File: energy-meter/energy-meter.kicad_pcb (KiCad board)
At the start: 2 copper layers, 82 x 62.5 mm, 74 parts, among them J1 Screw_Terminal_01x04, J2 Conn_01x03, J3 I2C OLED Display, etc., K1 G5RL-U1A-E, K2 DNP / HF3FF/005-1HST, P1 PineNut, Q1 AP3400, T1 AP-2500, T2 BV 202 0154, T3 DNP / AP-2500, U1 L9110S, U11 SLG47004, U2 MCP6V96T-E/OT, U9 GD32VF103

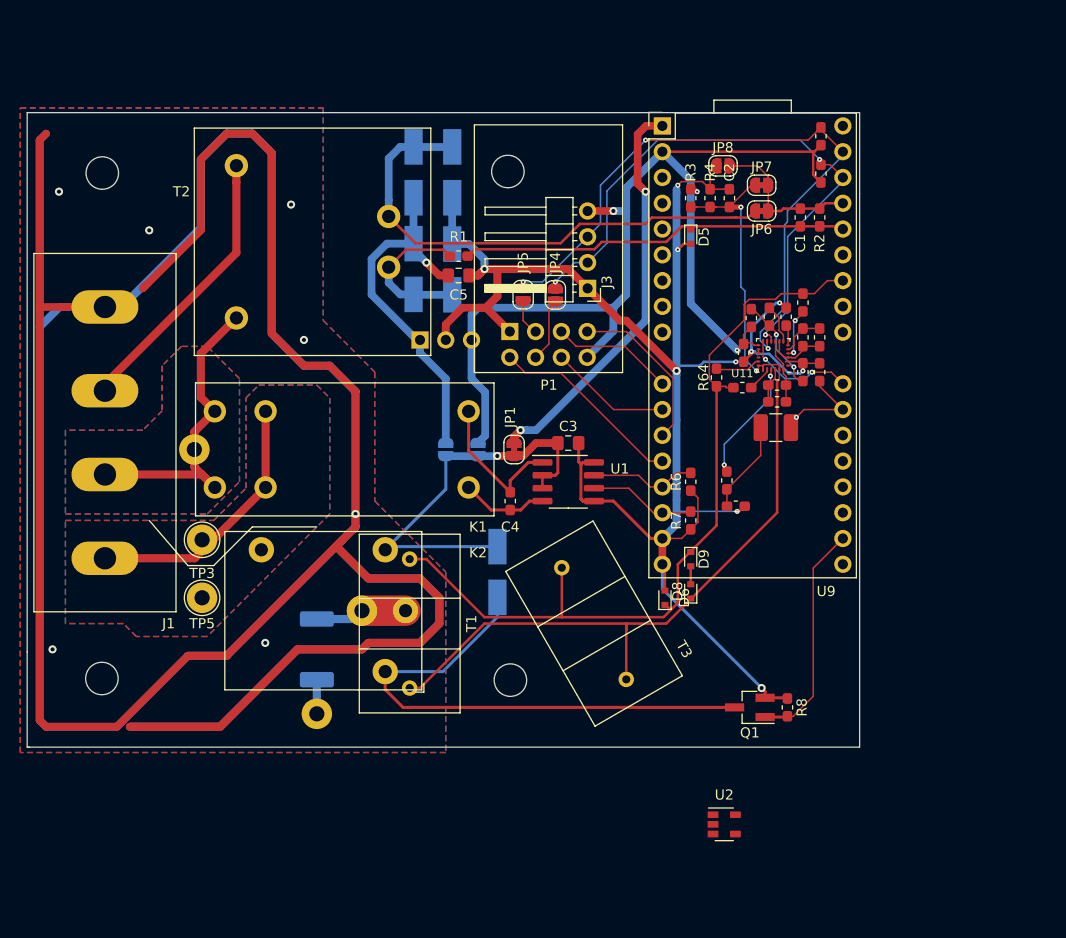
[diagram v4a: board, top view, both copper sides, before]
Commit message: use solid state relays for calibration
That way, we have enough space for two of them. The alternative relay
shares space with the other relay because only one of them will be used.
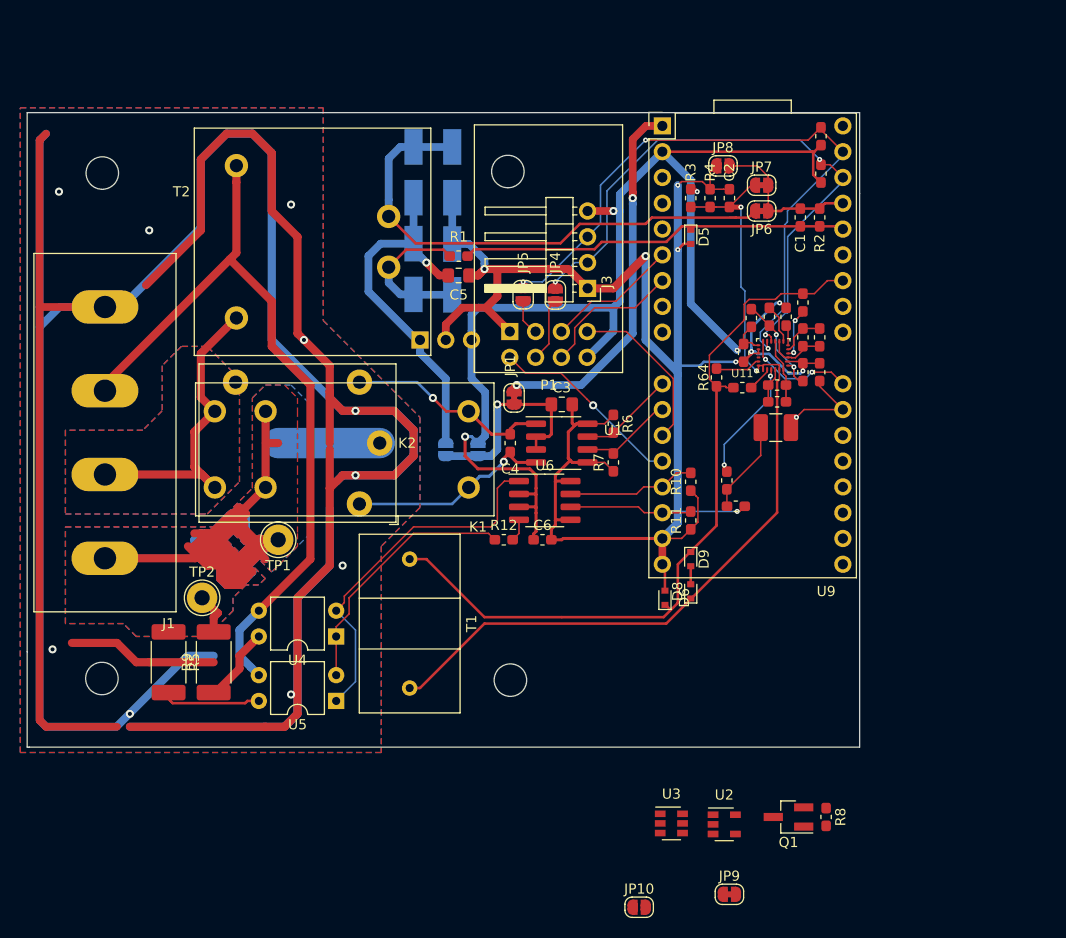
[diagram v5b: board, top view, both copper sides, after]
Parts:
- removed D7: D_Schottky, Diode_SMD:D_SMA_Handsoldering
- removed T3: DNP / AP-2500, energy-meter:AP-2500
- removed the TP2 at (119.5, 126.5)
- removed TP3, TP4: TestPoint, TestPoint:TestPoint_THTPad_D3.0mm_Drill1.5mm
- added C6: 100n, Capacitor_SMD:C_0603_1608Metric_Pad1.05x0.95mm_HandSolder, F.Cu at (153.8, 135.4)
- added JP10: SolderJumper_2_Open, Jumper:SolderJumper-2_P1.3mm_Open_RoundedPad1.0x1.5mm, F.Cu at (163.3, 171.6)
- added JP9: SolderJumper_2_Bridged, Jumper:SolderJumper-2_P1.3mm_Bridged_RoundedPad1.0x1.5mm, F.Cu at (172.2, 170.3)
- added NT2: Net-Tie_2, NetTie:NetTie-2_SMD_Pad2.0mm, F.Cu at (122.1, 134.8)
- added NT3: Net-Tie_2, NetTie:NetTie-2_SMD_Pad2.0mm, F.Cu at (124.6, 137.3)
- added NT4: Net-Tie_2, NetTie:NetTie-2_SMD_Pad2.0mm, B.Cu at (122.1, 134.8)
- added NT5: Net-Tie_2, NetTie:NetTie-2_SMD_Pad2.0mm, B.Cu at (124.6, 137.3)
- added R10: 10k, Resistor_SMD:R_0603_1608Metric_Pad1.05x0.95mm_HandSolder, F.Cu at (168.4, 129.7)
- added R11: 10k, Resistor_SMD:R_0603_1608Metric_Pad1.05x0.95mm_HandSolder, F.Cu at (168.4, 133.5)
- added R12: 120R, Resistor_SMD:R_0603_1608Metric_Pad1.05x0.95mm_HandSolder, F.Cu at (150.0, 135.4)
- added R9: 470kOhm, 0.1W, 1%, Resistor_SMD:R_2512_6332Metric_Pad1.52x3.35mm_HandSolder, F.Cu at (121.4, 147.5)
- added U3: TS5A3159ADBVR, Package_TO_SOT_SMD:SOT-23-6, F.Cu at (166.5, 163.3)
- added U4: EPR211A354001EZ, Package_DIP:DIP-4_W7.62mm, F.Cu at (133.5, 144.9)
- added U5: EPR211A354001EZ, Package_DIP:DIP-4_W7.62mm, F.Cu at (133.5, 151.3)
- added U6: L9110S, Package_SO:SOP-8_3.76x4.96mm_P1.27mm, F.Cu at (154.1, 131.5)
- R5: value 39kOhm, 2W, 1% -> 27kOhm, 2W, 1%; moved to F.Cu
- TP1: moved to F.Cu
- moved K2 16.7 mm to (129.7, 125.9)
- moved R5 14.7 mm to (117.0, 147.5)
- moved Q1 11.4 mm to (178.1, 162.7)
- moved R8 11.4 mm to (181.8, 162.7)
- moved TP1 10.8 mm to (127.8, 135.4)
- moved R6 9.52 mm to (160.8, 124.0), turned to 270 degrees
- moved R7 9.52 mm to (160.8, 127.8)
- moved C4 5.71 mm to (150.7, 125.9)
- moved JP1 5.08 mm to (151.0, 121.4)
- moved C3 3.86 mm to (155.7, 122.1)
- moved U1 3.86 mm to (155.7, 125.9)
- renumbered NT2 to NT1, TP5 to TP2
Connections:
- J1 pad 4: L_OUT -> L_OUT2
- K2 pad 1: Net-(K2-Pad1) -> L_OUT
- K2 pad 14: Net-(K2-Pad1) -> L_OUT
- K2 pad 2: /VCC_COIL -> /coil+
- K2 pad 6: Net-(D7-Pad2) -> /coil-
- K2 pad 7: L_OUT -> L_IN
- K2 pad 8: L_OUT -> L_IN
- Q1 pad 1: /RELAY2 -> /Calibration circuits for 230V/RELAY2
- Q1 pad 3: Net-(D7-Pad2) -> Net-(Q1-Pad3)
- R5 pad 2: Net-(K2-Pad1) -> L_OUT2
- R8 pad 2: /RELAY2 -> /Calibration circuits for 230V/RELAY2
- TP1 pad 1: Net-(K2-Pad1) -> L_OUT
- TP2 pad 1: L_OUT -> L_OUT2
- U9 pad 11: /PINENUT_IO8_BOOT -> /RELAY_SET
- U9 pad 12: /PINENUT_RST -> /RELAY_RESET
- U9 pad 15: /RELAY_SET -> /ENA_470k
- U9 pad 16: /RELAY_RESET -> /ENA_27k
- U9 pad 6: Net-(U9-Pad6) -> /PINENUT_IO8_BOOT
- U9 pad 7: Net-(U9-Pad7) -> /PINENUT_RST
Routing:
- net L_OUT2: track 0.00 -> 73.0 mm
- net Net-(D7-Pad2): track 52.1 -> 0.00 mm
- net N: track 27.5 -> 75.5 mm
- net PE: track 444.8 -> 408.0 mm, vias 7 -> 10
- net Net-(U4-Pad2): track 0.00 -> 36.0 mm
- net Net-(R12-Pad1): track 0.00 -> 25.4 mm
- net L_OUT: track 26.2 -> 50.0 mm
- net /RELAY2: track 22.3 -> 0.00 mm
- net +3V3: track 103.5 -> 124.0 mm, vias 3 -> 4
- net /VCC_COIL: track 40.3 -> 20.9 mm
- net /ENA_470k: track 0.00 -> 12.7 mm
- net /ENA_27k: track 0.00 -> 12.1 mm
- net /coil-: track 8.56 -> 19.7 mm, vias 0 -> 1
- net Net-(K2-Pad1): track 9.08 -> 0.00 mm
- net Net-(R9-Pad1): track 0.00 -> 8.11 mm
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- added copper zone on B.Cu, net L_OUT2
- added copper zone on F.Cu, net L_OUT2

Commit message: add opamps
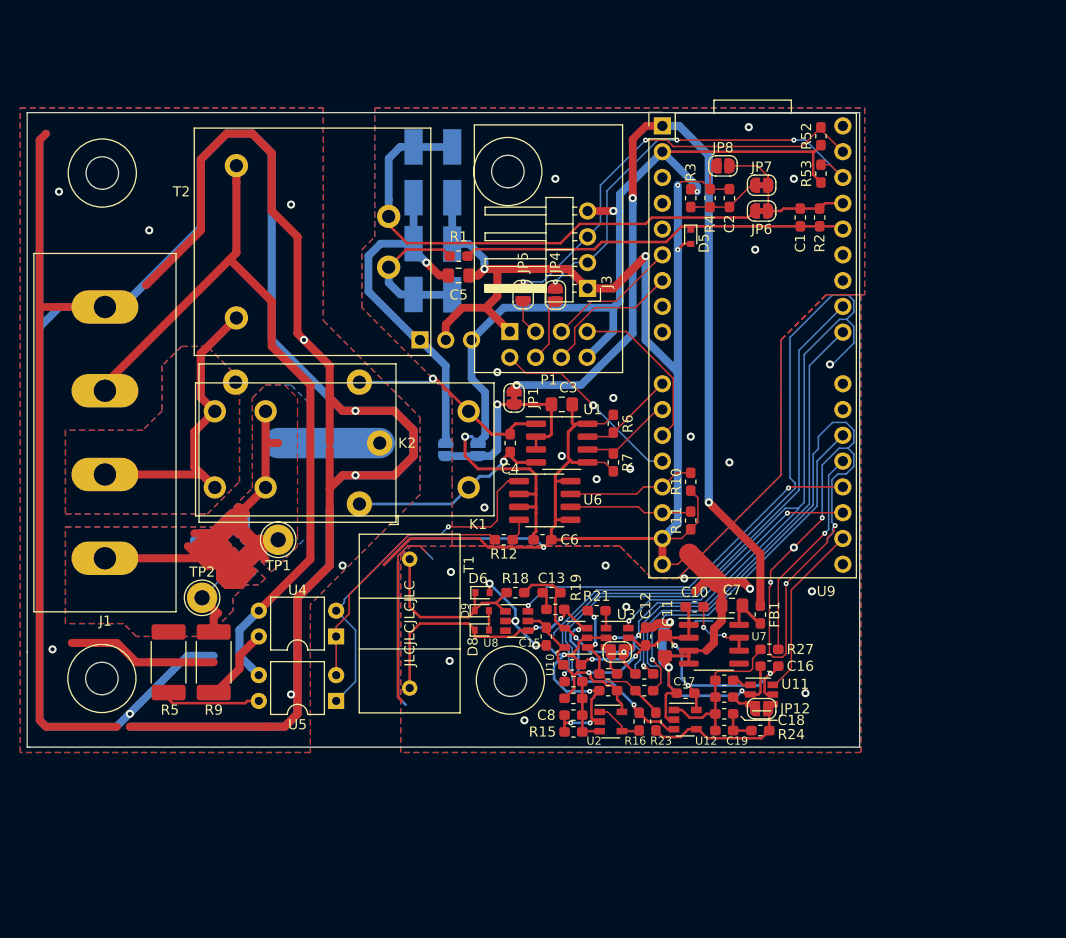
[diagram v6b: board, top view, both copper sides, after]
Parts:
- removed C66, C68: 100n, Capacitor_SMD:C_0603_1608Metric_Pad1.05x0.95mm_HandSolder
- removed C77, C78: 4.7p, Capacitor_SMD:C_0603_1608Metric_Pad1.05x0.95mm_HandSolder
- removed C84: 270p, 1%, Capacitor_SMD:C_0603_1608Metric_Pad1.05x0.95mm_HandSolder
- removed FB2: 600R, 0.5A, Inductor_SMD:L_0603_1608Metric_Pad1.05x0.95mm_HandSolder
- removed JP10: SolderJumper_2_Open, Jumper:SolderJumper-2_P1.3mm_Open_RoundedPad1.0x1.5mm
- removed JP9: SolderJumper_2_Bridged, Jumper:SolderJumper-2_P1.3mm_Bridged_RoundedPad1.0x1.5mm
- removed L4: 470u, Inductor_SMD:L_1210_3225Metric_Pad1.42x2.65mm_HandSolder
- removed Q1: AP3400, Package_TO_SOT_SMD:SOT-23_Handsoldering
- removed R64: 50k, 0.1%, Resistor_SMD:R_0603_1608Metric_Pad1.05x0.95mm_HandSolder
- removed R66: 1k, Resistor_SMD:R_0603_1608Metric_Pad1.05x0.95mm_HandSolder
- removed R72, R73, R8: 10k, Resistor_SMD:R_0603_1608Metric_Pad1.05x0.95mm_HandSolder
- removed R74, R75: 47k, Resistor_SMD:R_0603_1608Metric_Pad1.05x0.95mm_HandSolder
- removed R85: 50R, 0.1%, Resistor_SMD:R_0603_1608Metric_Pad1.05x0.95mm_HandSolder
- removed R90, R91: 1k, 1%, Resistor_SMD:R_0603_1608Metric_Pad1.05x0.95mm_HandSolder
- added C10: 10n, Capacitor_SMD:C_0603_1608Metric_Pad1.05x0.95mm_HandSolder, F.Cu at (168.8, 142.0)
- added C11: 10u, Capacitor_SMD:C_0805_2012Metric_Pad1.15x1.40mm_HandSolder, F.Cu at (165.9, 145.8)
- added C12: 100n, Capacitor_SMD:C_0603_1608Metric_Pad1.05x0.95mm_HandSolder, F.Cu at (164.0, 144.9)
- added C13: 10n, Capacitor_SMD:C_0603_1608Metric_Pad1.05x0.95mm_HandSolder, F.Cu at (154.7, 140.6)
- added C14: 100n, Capacitor_SMD:C_0603_1608Metric_Pad1.05x0.95mm_HandSolder, F.Cu at (156.7, 147.7)
- added C15: 100n, Capacitor_SMD:C_0603_1608Metric_Pad1.05x0.95mm_HandSolder, F.Cu at (154.2, 144.9)
- added C16: 100n, Capacitor_SMD:C_0603_1608Metric_Pad1.05x0.95mm_HandSolder, F.Cu at (176.2, 147.9)
- added C17: 100n, Capacitor_SMD:C_0603_1608Metric_Pad1.05x0.95mm_HandSolder, F.Cu at (167.9, 150.5)
- added C18: 270p, 1%, Capacitor_SMD:C_0603_1608Metric_Pad1.05x0.95mm_HandSolder, F.Cu at (171.7, 152.6)
- added C19: 270p, 1%, Capacitor_SMD:C_0603_1608Metric_Pad1.05x0.95mm_HandSolder, F.Cu at (171.7, 154.2)
- added C7: 10u, Capacitor_SMD:C_0805_2012Metric_Pad1.15x1.40mm_HandSolder, F.Cu at (172.5, 141.9)
- added C8: 100n, Capacitor_SMD:C_0603_1608Metric_Pad1.05x0.95mm_HandSolder, F.Cu at (156.9, 152.7)
- added C9: 100n, Capacitor_SMD:C_0603_1608Metric_Pad1.05x0.95mm_HandSolder, F.Cu at (160.3, 150.3)
- added FB1: 600R, 0.5A, Inductor_SMD:L_0603_1608Metric_Pad1.05x0.95mm_HandSolder, F.Cu at (175.3, 142.8)
- added JP11: SolderJumper_2_Open, Jumper:SolderJumper-2_P1.3mm_Open_RoundedPad1.0x1.5mm, F.Cu at (161.2, 146.5)
- added JP12: SolderJumper_2_Open, Jumper:SolderJumper-2_P1.3mm_Open_RoundedPad1.0x1.5mm, F.Cu at (175.4, 152.0)
- added R13: 0R, Resistor_SMD:R_0603_1608Metric_Pad1.05x0.95mm_HandSolder, F.Cu at (156.9, 149.4)
- added R14: 10k, 1%, Resistor_SMD:R_0603_1608Metric_Pad1.05x0.95mm_HandSolder, F.Cu at (156.9, 151.0)
- added R15: 10k, 1%, Resistor_SMD:R_0603_1608Metric_Pad1.05x0.95mm_HandSolder, F.Cu at (156.9, 154.3)
- added R16: 0R, Resistor_SMD:R_0603_1608Metric_Pad1.05x0.95mm_HandSolder, F.Cu at (163.3, 153.3)
- added R17: 100k, Resistor_SMD:R_0603_1608Metric_Pad1.05x0.95mm_HandSolder, F.Cu at (163.9, 148.6)
- added R18: 10R, Resistor_SMD:R_0603_1608Metric_Pad1.05x0.95mm_HandSolder, F.Cu at (151.2, 140.6)
- added R19: 10R, Resistor_SMD:R_0603_1608Metric_Pad1.05x0.95mm_HandSolder, F.Cu at (155.1, 142.3)
- added R20: 220R, 1%, Resistor_SMD:R_0603_1608Metric_Pad1.05x0.95mm_HandSolder, F.Cu at (160.3, 148.6)
- added R21: 220k, 1%, Resistor_SMD:R_0603_1608Metric_Pad1.05x0.95mm_HandSolder, F.Cu at (159.2, 142.4)
- added R22: 1k, 1%, Resistor_SMD:R_0603_1608Metric_Pad1.05x0.95mm_HandSolder, F.Cu at (163.9, 150.3)
- added R23: 1k, 1%, Resistor_SMD:R_0603_1608Metric_Pad1.05x0.95mm_HandSolder, F.Cu at (165.0, 153.3)
- added R24: 1k, 1%, Resistor_SMD:R_0603_1608Metric_Pad1.05x0.95mm_HandSolder, F.Cu at (175.3, 154.2)
- added R25: 10k, 1%, Resistor_SMD:R_0603_1608Metric_Pad1.05x0.95mm_HandSolder, F.Cu at (171.7, 150.9)
- added R26: 100k, 1%, Resistor_SMD:R_0603_1608Metric_Pad1.05x0.95mm_HandSolder, F.Cu at (171.7, 149.3)
- added R27: 1k, 1%, Resistor_SMD:R_0603_1608Metric_Pad1.05x0.95mm_HandSolder, F.Cu at (176.2, 146.2)
- added U10: MCP6V96T-E/OT, Package_TO_SOT_SMD:SOT-23-5, F.Cu at (157.1, 145.1)
- added U12: MCP6V96T-E/OT, Package_TO_SOT_SMD:SOT-23-5, F.Cu at (167.9, 153.1)
- added U7: LP2951-3.3_SOIC, Package_SO:SOIC-8_3.9x4.9mm_P1.27mm, F.Cu at (170.7, 145.7)
- added U8: TS5A3159ADBVR, Package_TO_SOT_SMD:SOT-23-6, F.Cu at (151.3, 143.4)
- NT1: footprint NetTie:NetTie-2_SMD_Pad0.5mm -> NetTie:NetTie-2_SMD_Pad2.0mm
- U11: value SLG47004 -> TS5A3159ADBVR; footprint glowstone:SLG47004 -> Package_TO_SOT_SMD:SOT-23-6
- moved NT1 35.7 mm to (169.7, 138.2), turned to 315 degrees
- moved U11 33.4 mm to (175.4, 150.7), turned to 0 degrees
- moved D9 21.2 mm to (147.9, 142.4), turned to 0 degrees
- moved D8 20.9 mm to (147.9, 144.3), turned to 0 degrees
- moved U3 19.0 mm to (161.2, 145.1)
- moved D6 18.0 mm to (147.9, 140.6), turned to 0 degrees
- moved U2 15.1 mm to (160.6, 153.3)
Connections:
- D6 pad 2: GND -> GNDA
- NT1 pad 1: /CURRENT1 -> GND
- NT1 pad 2: /BIAS -> GNDA
- U11 pad 1: /Modified LCR Meter/VDDA2 -> Net-(R26-Pad2)
- U11 pad 2: GND -> GNDA
- U11 pad 3: Net-(C77-Pad2) -> Net-(JP12-Pad2)
- U11 pad 5: Net-(C77-Pad1) -> VDDA
- U11 pad 6: Net-(R75-Pad1) -> /ENA_100x
- U2 pad 1: Net-(U2-Pad1) -> Net-(R16-Pad2)
- U2 pad 2: Net-(U2-Pad2) -> GNDA
- U2 pad 4: Net-(U2-Pad4) -> Net-(R16-Pad2)
- U2 pad 5: Net-(U2-Pad5) -> VDDA
- U3 pad 2: Net-(U3-Pad2) -> GNDA
- U3 pad 5: Net-(U3-Pad5) -> VDDA
- U3 pad 6: Net-(U3-Pad6) -> /ENA_1000x
- U9 pad 20: /RELAY2 -> /ENA_100x
- U9 pad 21: Net-(U9-Pad21) -> /ENA_1000x
- U9 pad 22: Net-(U9-Pad22) -> /SHORT_CURRENT
- U9 pad 23: Net-(U9-Pad23) -> /CURRENT_OUT1
- U9 pad 24: Net-(U9-Pad24) -> /CURRENT_OUT0
- U9 pad 25: /OP1_OUT_F -> Net-(U9-Pad25)
- U9 pad 26: /TEMP1 -> Net-(U9-Pad26)
- U9 pad 28: /DAC0 -> /TUNE_OFFSET
- U9 pad 29: /DAC1 -> /BIAS_MCU
- U9 pad 30: /CURRENT0 -> Net-(U9-Pad30)
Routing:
- net GNDA: track 0.00 -> 370.5 mm, vias 0 -> 28
- net VDDA: track 0.00 -> 57.0 mm, vias 0 -> 5
- net /CURRENT0: track 75.3 -> 18.8 mm
- net /BIAS_MCU: track 0.00 -> 54.5 mm, vias 0 -> 1
- net +5V: track 36.5 -> 88.7 mm, vias 2 -> 3
- net /TUNE_OFFSET: track 0.00 -> 45.0 mm, vias 0 -> 1
- net /SHORT_CURRENT: track 0.00 -> 36.4 mm, vias 0 -> 2
- net /CURRENT_OUT0: track 0.00 -> 36.1 mm, vias 0 -> 1
- net /CURRENT1: track 77.9 -> 44.4 mm, vias 2 -> 4
- net /ENA_1000x: track 0.00 -> 26.2 mm, vias 0 -> 2
- net /SDA: track 65.6 -> 42.3 mm, vias 3 -> 2
- net +3V3: track 124.0 -> 100.7 mm, vias 4 -> 3
- net /CURRENT_OUT1: track 0.00 -> 21.3 mm, vias 0 -> 1
- net Net-(C13-Pad2): track 0.00 -> 18.5 mm, vias 0 -> 2
- net /ENA_100x: track 0.00 -> 17.4 mm
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- added copper zone on B.Cu, net GND
- added copper zone on F.Cu, net GND
- added copper zone on B.Cu, net GNDA
- added copper zone on F.Cu, net GNDA
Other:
- board text added: "JLCJLCJLCJLC"

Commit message: add logos, increase distance to SELV, add PDFs and Gerbers
Lot's of whitespace changes, unfortunately.
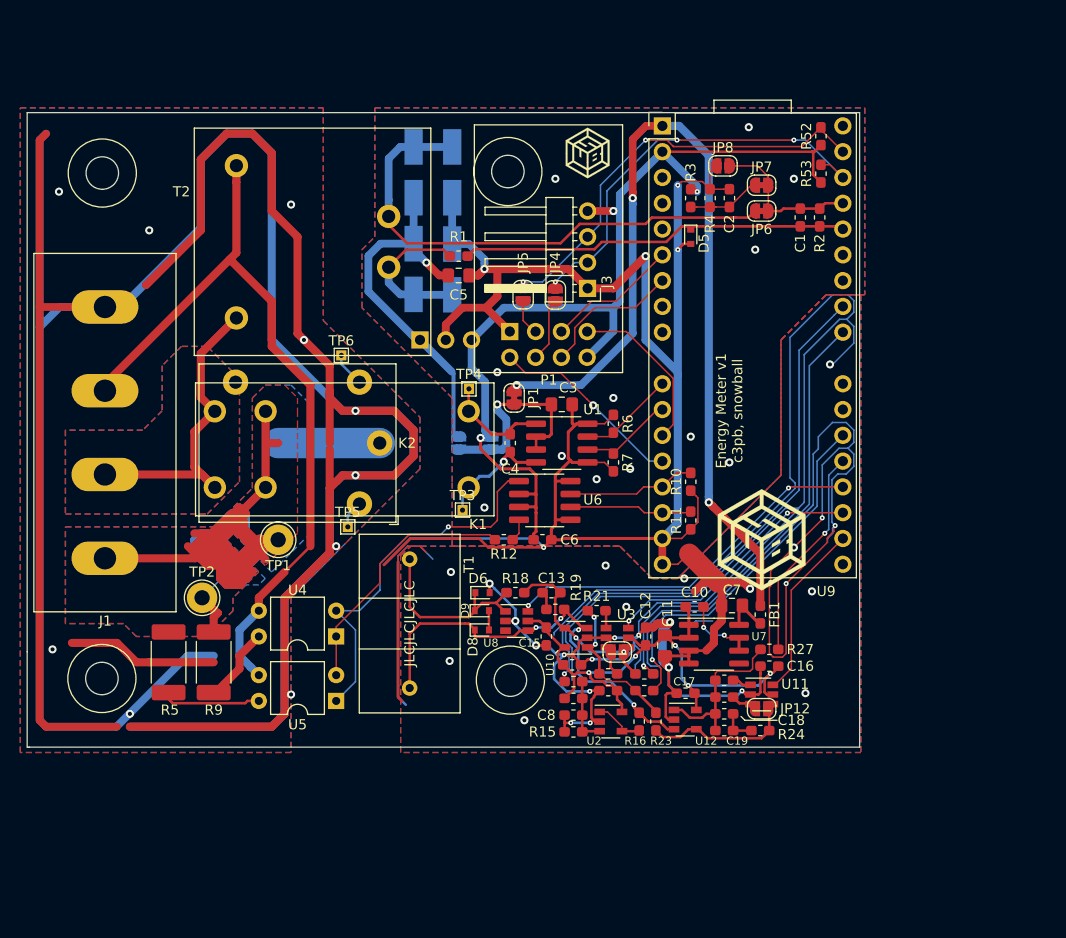
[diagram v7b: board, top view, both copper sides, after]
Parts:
- added G***: LOGO, energy-meter:subraum_40mm, B.Cu at (165.3, 135.4)
- added G***: LOGO, energy-meter:subraum_5mm, F.Cu at (158.3, 97.3)
- added G***: LOGO, energy-meter:subraum_10mm, F.Cu at (175.4, 135.4)
- added TP3: TestPoint, TestPoint:TestPoint_THTPad_1.0x1.0mm_Drill0.5mm, F.Cu at (146.0, 132.5)
- added TP4: TestPoint, TestPoint:TestPoint_THTPad_1.0x1.0mm_Drill0.5mm, F.Cu at (146.6, 120.6)
- added TP5: TestPoint, TestPoint:TestPoint_THTPad_1.0x1.0mm_Drill0.5mm, F.Cu at (134.6, 134.1)
- added TP6: TestPoint, TestPoint:TestPoint_THTPad_1.0x1.0mm_Drill0.5mm, F.Cu at (134.0, 117.2)
- moved JP2 1.42 mm to (148.7, 125.9)
- moved JP3 1.42 mm to (145.6, 125.9)
- turned G*** to 180 degrees
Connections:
- K2 pad 2: /coil+ -> Net-(K2-Pad2)
- K2 pad 6: /coil- -> Net-(K2-Pad6)
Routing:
- net /coil+: track 19.9 -> 10.0 mm, vias 1 -> 0
- net /coil-: track 19.7 -> 10.8 mm
- net Net-(K2-Pad2): track 0.00 -> 3.37 mm
- net +3V3: track 100.7 -> 97.5 mm
- net Net-(K2-Pad6): track 0.00 -> 2.76 mm
- net Net-(U4-Pad2): track 35.6 -> 36.9 mm

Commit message: remove optional parts, increase distance between conductors on primary side
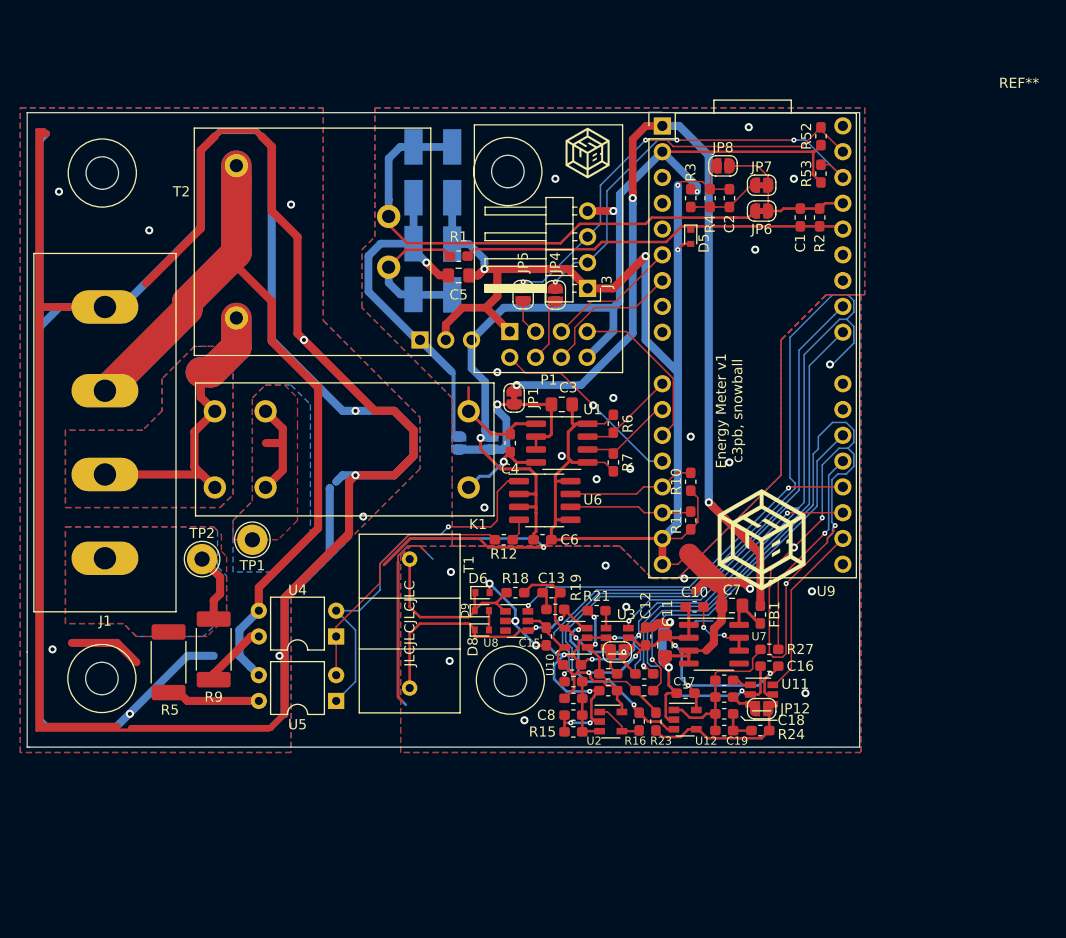
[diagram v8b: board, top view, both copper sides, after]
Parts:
- removed K2: DNP / HF3FF/005-1HST, energy-meter:Relay_HF3FF_005
- removed NT2, NT3, NT4, NT5: Net-Tie_2, NetTie:NetTie-2_SMD_Pad2.0mm
- removed TP3, TP4, TP5, TP6: TestPoint, TestPoint:TestPoint_THTPad_1.0x1.0mm_Drill0.5mm
- moved TP2 3.81 mm to (120.3, 137.3)
- moved TP1 2.54 mm to (125.2, 135.4)
- moved R9 1.27 mm to (121.4, 146.2)
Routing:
- net L_OUT2: track 78.2 -> 6.90 mm
- net PE: track 408.4 -> 475.4 mm
- net L_OUT: track 50.0 -> 10.1 mm
- net N: track 75.5 -> 104.2 mm
- net L_IN: track 31.7 -> 39.7 mm
- net Net-(K2-Pad2): track 3.37 -> 0.00 mm
- net Net-(K2-Pad6): track 2.76 -> 0.00 mm
- net /coil-: track 10.8 -> 8.30 mm
- net Net-(R9-Pad1): track 8.11 -> 6.55 mm
